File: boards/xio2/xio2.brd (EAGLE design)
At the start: 170 x 100 mm, 367 parts, among them IC1 MCP604SL, J1 12401598E4#2A, Q1 BSS138, Q2 BSS138, Q3 BC817-16LT3G, Q4 BC817-16LT3G, Y2 FA-238 25.0000MB-K3

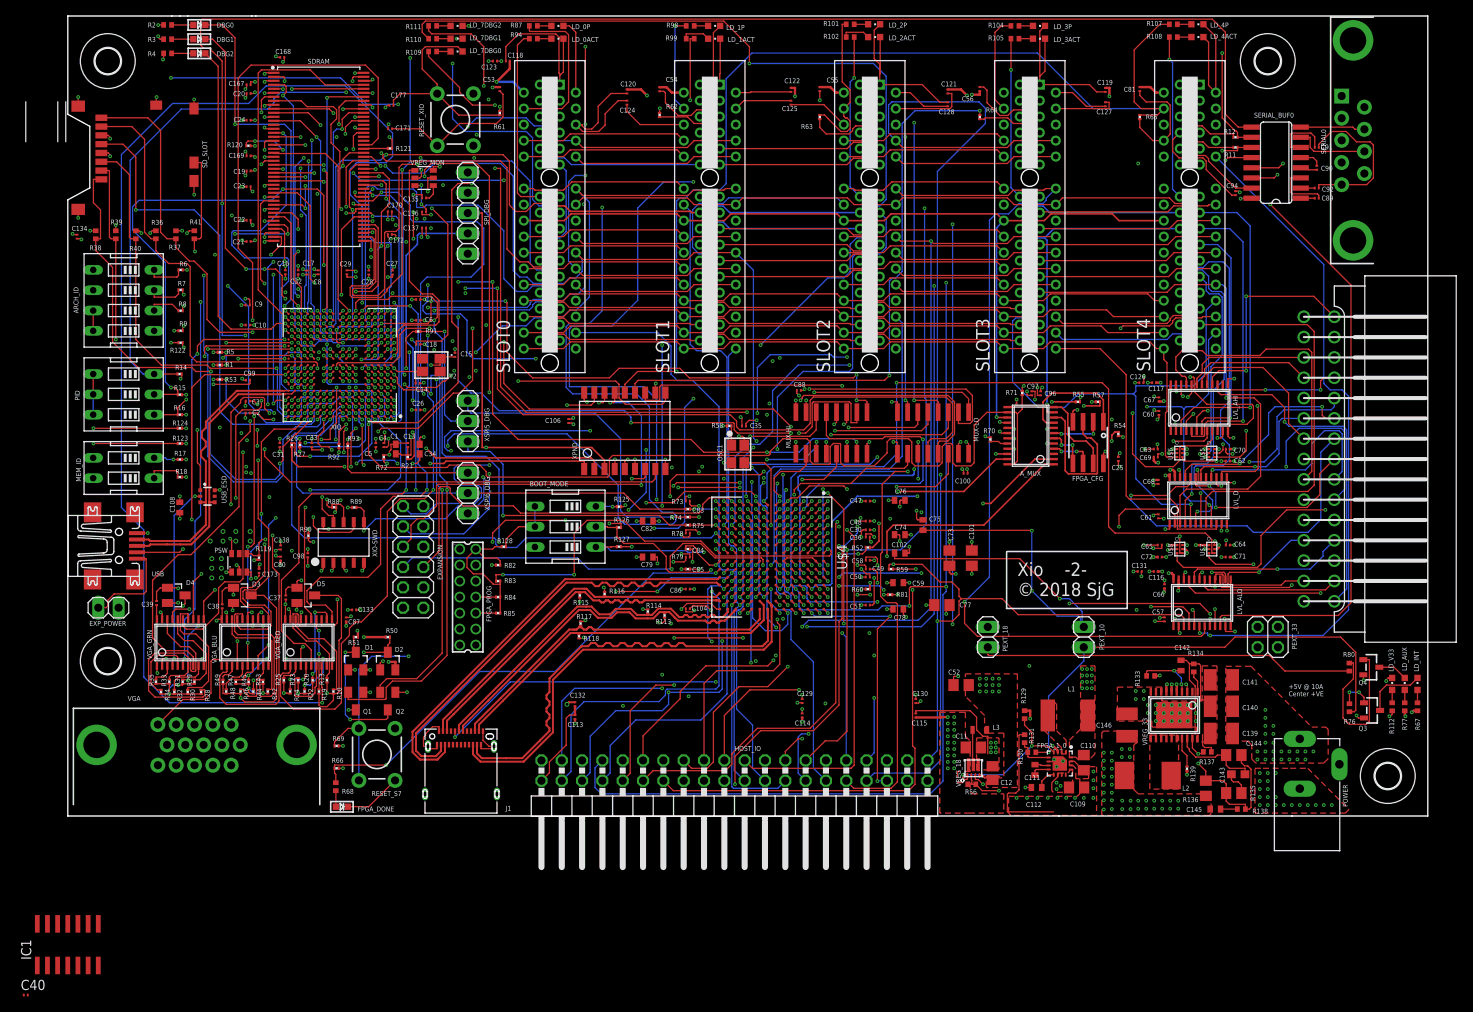
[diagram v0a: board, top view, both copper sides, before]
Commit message: - Move to a 64MB RAM chip, which meant using a 16-bit port expander  - Add an op-amp to the output stage of the VGA connector  - change the bus drivers to drive 5v rather than 3.3v on the VGA
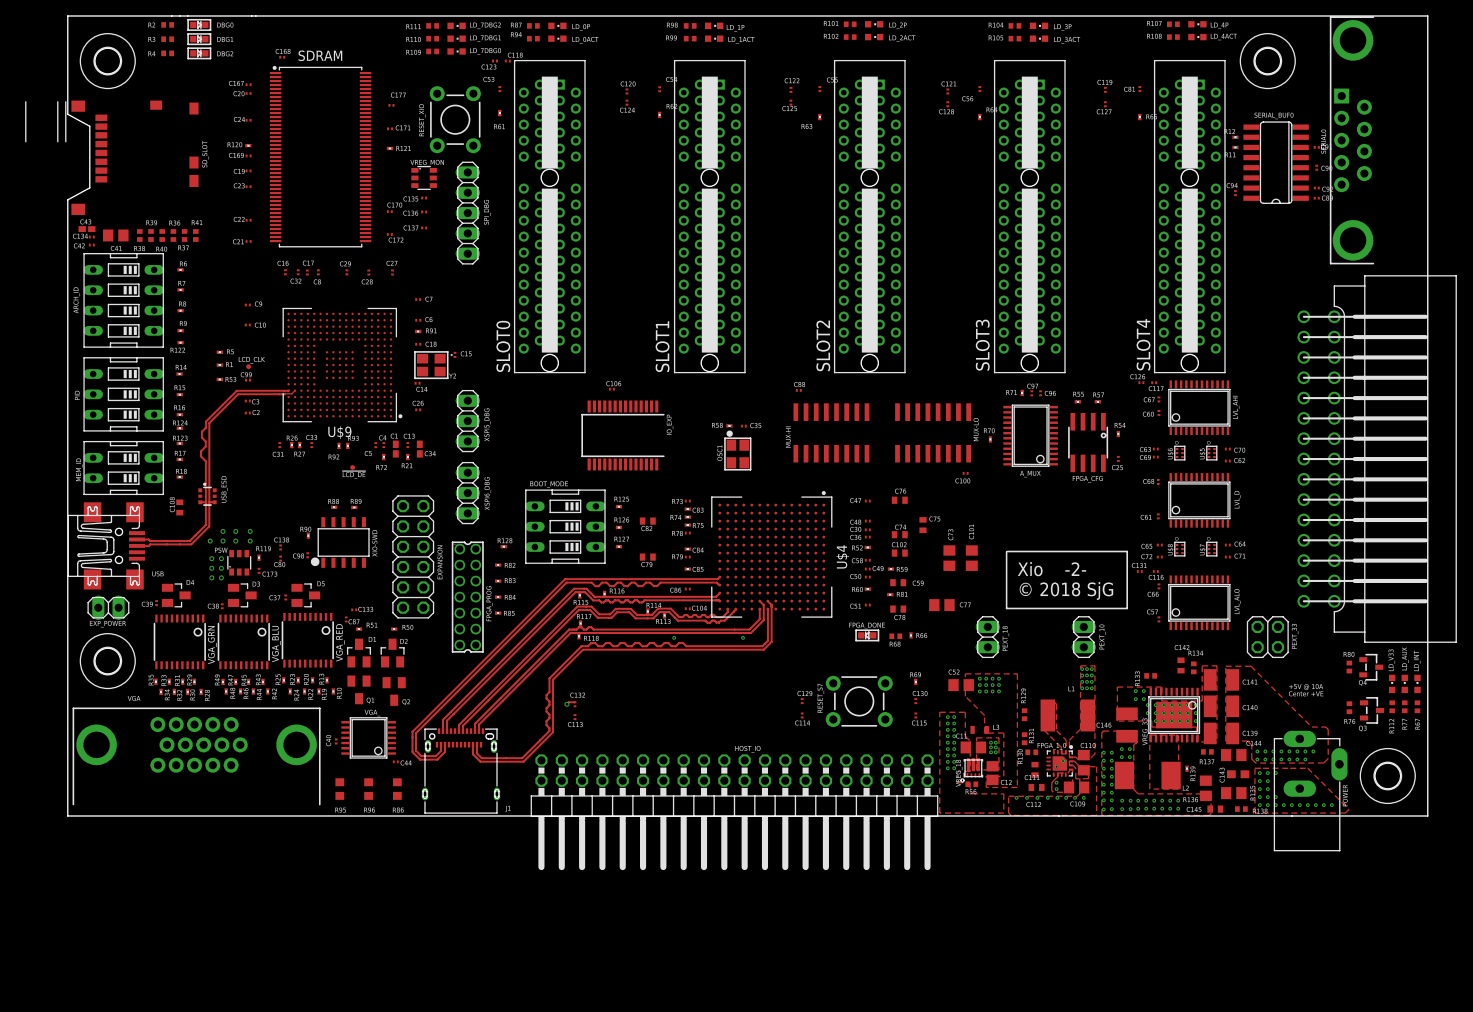
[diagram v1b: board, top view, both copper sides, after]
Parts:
- removed IC1: MCP604SL, linear:SO14
- removed XPND: MCP23S08, sjg-logic:SO18-1
- added !LCD_DE!, LCD_CLK: PTR1TP06R, testpad:TP06R
- added C41: 22uF, rcl:C0805
- added C42: 1uF, rcl:C0201
- added C43: 10uF, rcl:C0402K
- added C44: 0.1uF, rcl:C0201
- added IO_EXP: MCP23S17T-E/SS, sjg-logic:SSOP28
- added R86, R95, R96: 68R, rcl:R0603
- added VGA_: MAX4382, sjg-opamp:TSSOP14
- SDRAM: value IS42S32800J -> IS42S32160F-7TLI
- VGA_BLU, VGA_GRN, VGA_RED: value SN74ALVC244PWR -> (none); device sjg-logic:TSSOP20 -> microbuilder:TSSOP20
- moved R66 73.7 mm to (105.4, 23.2), turned to 270 degrees
- moved R69 72.8 mm to (106.0, 17.4), turned to 90 degrees
- moved R68 72.5 mm to (103.5, 23.1), turned to 0 degrees
- moved FPGA_DONE 69.1 mm to (99.9, 23.2), turned to 90 degrees
- moved RESET_S7 60.7 mm to (98.9, 15.0), turned to 180 degrees
- moved C40 50.1 mm to (33.5, 9.95), turned to 90 degrees
- moved C106 6.71 mm to (68.0, 54.0), turned to 0 degrees
- moved R38 5.51 mm to (9.00, 73.2)
- moved R39 4.40 mm to (10.4, 73.2)
- moved R40 3.30 mm to (11.8, 73.2)
- moved R36 2.19 mm to (13.2, 73.2)
- moved C134 1.84 mm to (3.00, 73.0), turned to 0 degrees
- moved Q1 1.46 mm to (36.4, 16.4)
- moved Q2 1.44 mm to (40.8, 16.2)
- moved R50 1.28 mm to (40.8, 24.0)
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- renumbered XIO to U$9
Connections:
- removed net EXT_IO2: EXPANSION.12, XPND.17
- new net LCDCLK: LCD_CLK.TP, U$9.F16
- new net N$10: R96.2, VGA.3
- new net N$25: R86.1, VGA_.6, VGA_.7
- new net N$37: R95.2, VGA.2
- new net N$53: !LCD_DE!.TP, U$9.D7
- new net SDRAM_A12: SDRAM.69, U$9.H16
- net !IO_EXP_IRQ!: now also IO_EXP.19, IO_EXP.20, U$9.D3; no longer U$9.H15, XPND.8
- net !IO_EXP_SEL!: now also IO_EXP.11, U$9.N2; no longer U$9.H16, XPND.7
- net !RESET!: now also IO_EXP.18; no longer XPND.6
- net !SPI_IRQ!: now also U$9.D2; no longer U$9.L2
- net +3V3: now also C41.1, C42.1, C43.1, IO_EXP.9; no longer C37.1, C38.1, C39.1, C40.1, D3.2, D4.2, D5.2, IC1.4, VGA_BLU.20, VGA_GRN.20, VGA_RED.20, XPND.18
- net +5V: now also C37.1, C38.1, C39.1, C40.1, C44.1, D3.2, D4.2, D5.2, VGA_.1, VGA_.2, VGA_.3, VGA_.4, VGA_BLU.1, VGA_BLU.20, VGA_GRN.1, VGA_GRN.20, VGA_RED.1, VGA_RED.20
- net ARCH0: now also IO_EXP.1; no longer U$9.T4
- net ARCH1: now also IO_EXP.2; no longer U$9.U4
- net ARCH2: now also IO_EXP.3; no longer U$9.C2
- net ARCH3: now also IO_EXP.4; no longer U$9.C1
- net EXT_IO0: now also IO_EXP.7; no longer XPND.15
- net EXT_IO1: now also IO_EXP.8; no longer XPND.16
- net GND: now also C41.2, C42.2, C43.2, C44.2, EXPANSION.12, IO_EXP.10, IO_EXP.15, IO_EXP.16, IO_EXP.17, VGA_.11; no longer IC1.11, VGA_BLU.1, VGA_GRN.1, VGA_RED.1, XPND.4, XPND.5, XPND.9
- net LCD_B1: now also VGA_BLU.3; no longer VGA_BLU.4
- net LCD_B2: now also VGA_BLU.4; no longer VGA_BLU.6
- net LCD_B3: now also VGA_BLU.5; no longer VGA_BLU.8
- net LCD_B4: now also VGA_BLU.6; no longer VGA_BLU.11
- net LCD_B5: now also VGA_BLU.7; no longer VGA_BLU.13
- net LCD_B6: now also VGA_BLU.8; no longer VGA_BLU.15
- net LCD_B7: now also VGA_BLU.9; no longer VGA_BLU.17
- net LCD_G1: now also VGA_GRN.3; no longer VGA_GRN.4
- net LCD_G2: now also VGA_GRN.4; no longer VGA_GRN.6
- net LCD_G3: now also VGA_GRN.5; no longer VGA_GRN.8
- net LCD_G4: now also VGA_GRN.6; no longer VGA_GRN.11
- net LCD_G5: now also VGA_GRN.7; no longer VGA_GRN.13
- net LCD_G6: now also VGA_GRN.8; no longer VGA_GRN.15
- net LCD_G7: now also VGA_GRN.9; no longer VGA_GRN.17
- net LCD_HS: now also U$9.H1; no longer U$9.H2
- net LCD_R1: now also VGA_RED.3; no longer VGA_RED.4
- net LCD_R2: now also VGA_RED.4; no longer VGA_RED.6
- net LCD_R3: now also VGA_RED.5; no longer VGA_RED.8
- net LCD_R4: now also VGA_RED.6; no longer VGA_RED.11
- net LCD_R5: now also VGA_RED.7; no longer VGA_RED.13
- net LCD_R6: now also VGA_RED.8; no longer VGA_RED.15
- net LCD_R7: now also VGA_RED.9; no longer VGA_RED.17
- net LCD_VS: now also U$9.H2; no longer U$9.H1
- net MEM0: now also IO_EXP.5; no longer U$9.D3
- net MEM1: now also IO_EXP.6; no longer U$9.D2
- net N$17: now also VGA_RED.16; no longer VGA_RED.14
- net N$18: now also VGA_RED.15; no longer VGA_RED.12
- net N$20: now also VGA_RED.14; no longer VGA_RED.9
- net N$21: now also VGA_RED.13; no longer VGA_RED.7
- net N$22: now also VGA_RED.12; no longer VGA_RED.5
- net N$23: now also VGA_RED.11; no longer VGA_RED.3
- net N$24: now also VGA_GRN.11; no longer VGA_GRN.3
- net N$26: now also VGA_GRN.12; no longer VGA_GRN.5
- net N$27: now also VGA_GRN.13; no longer VGA_GRN.7
- net N$34: now also VGA_GRN.14; no longer VGA_GRN.9
- net N$35: now also VGA_GRN.15; no longer VGA_GRN.12
- net N$36: now also VGA_GRN.16; no longer VGA_GRN.14
- net N$38: now also VGA_GRN.17; no longer VGA_GRN.16
- net N$40: now also VGA_BLU.11; no longer VGA_BLU.3
- net N$41: now also VGA_BLU.12; no longer VGA_BLU.5
- net N$42: now also VGA_BLU.13; no longer VGA_BLU.7
- net N$43: now also VGA_BLU.14; no longer VGA_BLU.9
- net N$44: now also VGA_BLU.15; no longer VGA_BLU.12
- net N$45: now also VGA_BLU.16; no longer VGA_BLU.14
- net N$46: now also VGA_BLU.17; no longer VGA_BLU.16
- net N$8: now also VGA_RED.17; no longer VGA_RED.16
- net PID0: now also IO_EXP.26; no longer U$9.E4
- net PID1: now also IO_EXP.27; no longer U$9.F4
- net PID2: now also IO_EXP.28; no longer U$9.H3
- net S0_PRESENT: now also IO_EXP.21; no longer XPND.10
- net S1_PRESENT: now also IO_EXP.22; no longer XPND.11
- net S2_PRESENT: now also IO_EXP.23; no longer XPND.12
- net S3_PRESENT: now also IO_EXP.24; no longer XPND.13
- net S4_PRESENT: now also IO_EXP.25; no longer XPND.14
- net SPI_CLK: now also IO_EXP.12; no longer XPND.1
- net SPI_IRQ0: now also U$9.H15; no longer U$9.G15
- net SPI_IRQ1: now also U$9.G15; no longer U$9.F16
- net SPI_MISO: now also IO_EXP.13; no longer XPND.2
- net SPI_MOSI: now also IO_EXP.14; no longer XPND.3
- net SPI_MUX_IN: now also U$9.P2; no longer U$9.D7
- net SPI_SS0: now also U$9.L2; no longer U$9.N2
- net SPI_SS1: now also U$9.T4; no longer U$9.P2
- net SPI_SS2: now also U$9.U4; no longer U$9.P3
- net SPI_SS3: now also U$9.C2; no longer U$9.T11
- net SPI_SS4: now also U$9.C1; no longer U$9.U13
- net VGA_B: now also R96.1, VGA_.13, VGA_.14; no longer IC1.8, IC1.9, VGA.3
- net VGA_BLUE: now also VGA_.12; no longer IC1.10
- net VGA_G: now also R95.1, VGA_.8, VGA_.9; no longer IC1.6, IC1.7, VGA.2
- net VGA_GRN: now also VGA_.10; no longer IC1.5
- net VGA_R: now also R86.2; no longer IC1.1, IC1.2
- net VGA_RED: now also VGA_.5; no longer IC1.3
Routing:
- net GND: track 673.6 -> 0.00 mm, vias 356 -> 60
- net HOST_A7: track 369.3 -> 0.00 mm, vias 10 -> 0
- net HOST_A3: track 312.5 -> 0.00 mm, vias 9 -> 0
- net HOST_A8: track 310.4 -> 0.00 mm, vias 9 -> 0
- net HOST_A0: track 308.7 -> 0.00 mm, vias 10 -> 0
- net HOST_A6: track 308.7 -> 0.00 mm, vias 7 -> 0
- net HOST_A5: track 296.1 -> 0.00 mm, vias 7 -> 0
- net HOST_A11: track 290.8 -> 0.00 mm, vias 8 -> 0
- net HOST_A14: track 282.7 -> 0.00 mm, vias 8 -> 0
- net HOST_A4: track 278.5 -> 0.00 mm, vias 6 -> 0
- net HOST_A1: track 277.5 -> 0.00 mm, vias 5 -> 0
- net HOST_A2: track 277.1 -> 0.00 mm, vias 9 -> 0
- net HOST_A10: track 273.0 -> 0.00 mm, vias 8 -> 0
- net HOST_A12: track 266.4 -> 0.00 mm, vias 8 -> 0
- net HOST_A9: track 257.8 -> 0.00 mm, vias 6 -> 0
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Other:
- board text added: "Silkscreen needs work SDRAM ought to be length-matched QSPI ought to be length-matched SD Card ought to be length-matched Maybe rotate stm ccw by 90 degrees ?"
- board text removed: "Silkscreen needs work SDRAM ought to be length-matched QSPI ought to be length-matched SD Card ought to be length-matched"

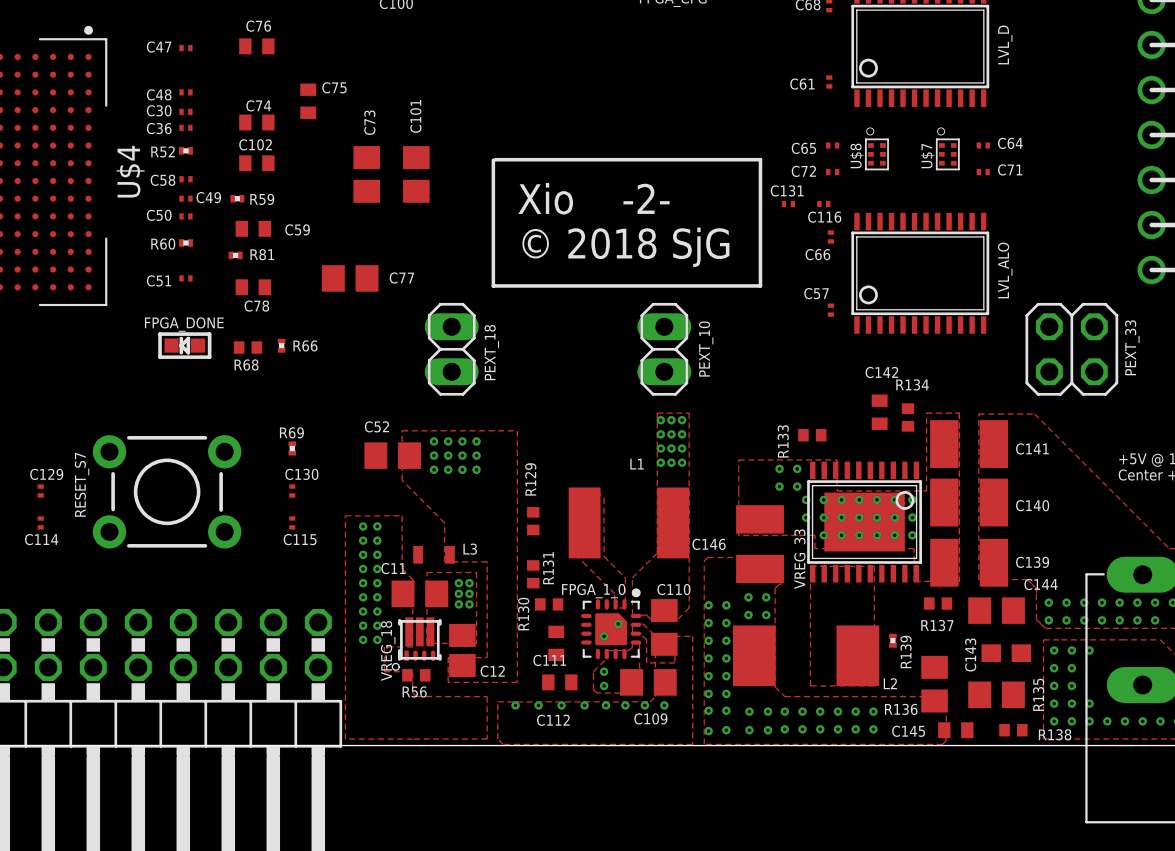
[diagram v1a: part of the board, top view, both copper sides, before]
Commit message: Tweaks to layout to get better part separation Rename XSPI bus properly Add NOSTUFF to fix ERC errors Add some notes to the schematic
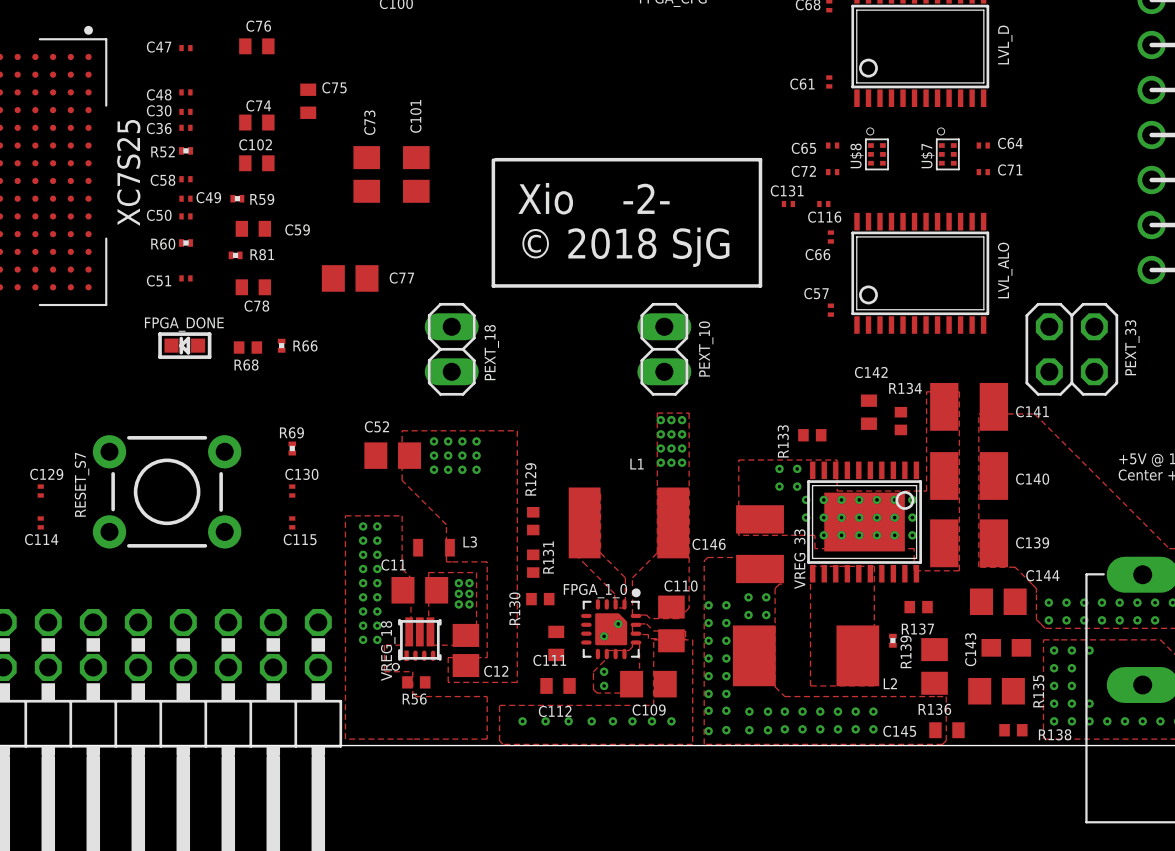
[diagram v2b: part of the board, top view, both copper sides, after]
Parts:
- moved C141 2.10 mm to (144.2, 19.8)
- moved C140 1.50 mm to (144.2, 15.8)
- moved R137 1.12 mm to (141.3, 8.45)
- moved C139 1.10 mm to (144.2, 12.1)
- moved R136 1.00 mm to (142.2, 5.10)
- moved R131 0.60 mm to (119.6, 10.9)
- moved C142 0.60 mm to (138.6, 19.4)
- moved R130 0.58 mm to (120.0, 8.90)
- moved C144 0.51 mm to (145.8, 8.75)
- moved C145 0.50 mm to (142.9, 1.50)
- moved C110 0.45 mm to (127.4, 7.50)
- moved R134 0.45 mm to (140.3, 18.9)
- moved L3 0.40 mm to (114.0, 11.8)
- moved R56 0.40 mm to (113.0, 4.20)
- moved C143 0.30 mm to (146.3, 6.15)
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- renumbered U$4 to XC7S25
